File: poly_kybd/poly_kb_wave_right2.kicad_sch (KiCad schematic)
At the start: 47 parts, among them J37 FH34SRJ-12S-0.5SH, J38 Conn_01x05, J39 FH12-30S-0.5SH, SW1 RotaryEncoder_Switch, U2 TD6811, U3 MT9700

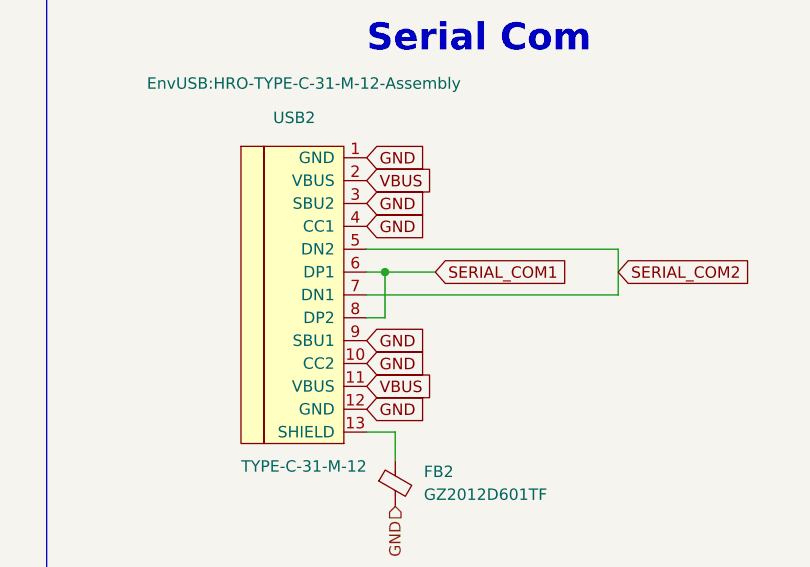
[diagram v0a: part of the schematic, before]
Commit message: Update PCB and plate to rev3 (disconnected vbus via bridge and removed polyfuse)
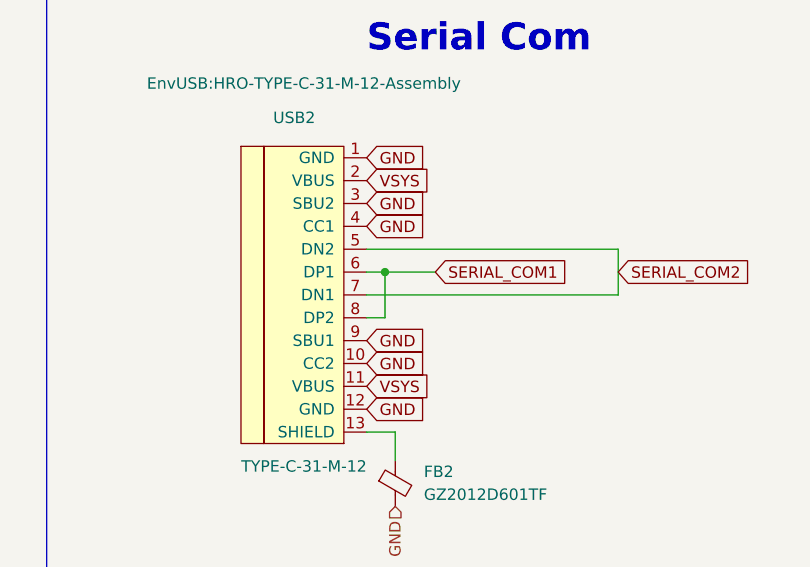
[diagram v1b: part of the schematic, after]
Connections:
- net VBUS: no longer USB2.11 (VBUS), USB2.2 (VBUS)
- net VSYS: now also USB2.11 (VBUS), USB2.2 (VBUS)
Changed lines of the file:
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@@
   (title_block
     (title "PolyKybd Split72 R")
-    (date "2023-06-22")
-    (rev "2.2")
+    (date "2023-09-19")
+    (rev "3")
   )
   (junction (at 259.08 219.075) (diameter 0) (color 0 0 0 0)
@@
     )
   )
-  (global_label "VBUS" (shape input) (at 410.21 358.14 0) (fields_autoplaced)
+  (global_label "VSYS" (shape input) (at 410.21 358.14 0) (fields_autoplaced)
     (effects (font (size 1.27 1.27)) (justify left))
-    (property "Intersheetrefs" "${INTERSHEET_REFS}" (at 417.5217 358.0606 0)
+    (property "Intersheetrefs" "${INTERSHEET_REFS}" (at 417.7914 358.14 0)
       (effects (font (size 1.27 1.27)) (justify left) hide)
     )
@@
     )
   )
-  (global_label "VBUS" (shape input) (at 410.21 381 0) (fields_autoplaced)
+  (global_label "VSYS" (shape input) (at 410.21 381 0) (fields_autoplaced)
     (effects (font (size 1.27 1.27)) (justify left))
-    (property "Intersheetrefs" "${INTERSHEET_REFS}" (at 417.5217 380.9206 0)
+    (property "Intersheetrefs" "${INTERSHEET_REFS}" (at 417.7914 381 0)
       (effects (font (size 1.27 1.27)) (justify left) hide)
     )

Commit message: Added latest gerber files, latest STLs and updated readme
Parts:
- R13: value 22k 0603 -> 12k 0603; JLC (none) -> C22790; MPN C31850 -> C22790
- R25: value 5.1K 0402 -> 10K 0402; MPN C25905 -> C25744
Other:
- note added: "Rset 27k -> ~250mA Max / Rset 22k -> ~310mA Max"
- note removed: "~250mA Max"
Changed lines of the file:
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@@
     (effects (font (size 3 3) (thickness 0.6) bold) (justify left bottom))
   )
-  (text "Increase for more current: Imax = 6.8k / RSet" (at 504.19 374.015 0)
+  (text "Increase for more current: Imax = 6.8k / RSet" (at 510.54 372.11 0)
     (effects (font (size 1.27 1.27) bold) (justify left bottom))
   )
@@
     (effects (font (size 3 3) (thickness 0.6) bold) (justify left bottom))
   )
-  (text "~250mA Max" (at 554.99 349.25 0)
+  (text "Rset 27k -> ~250mA Max / Rset 22k -> ~310mA Max" (at 500.38 375.285 0)
     (effects (font (size 1.27 1.27)) (justify left bottom))
   )
@@
       (effects (font (size 1.27 1.27)))
     )
-    (property "Value" "5.1K 0402" (at 490.855 369.57 90)
+    (property "Value" "10K 0402" (at 490.855 369.57 90)
       (effects (font (size 1.27 1.27)))
     )
@@
       (effects (font (size 1.27 1.27)) hide)
     )
-    (property "MPN" "C25905" (at 492.76 363.22 0)
+    (property "MPN" "C25744" (at 492.76 363.22 0)
       (effects (font (size 1.27 1.27)) hide)
     )
@@
       (effects (font (size 1.27 1.27)))
     )
-    (property "Value" "22k 0603" (at 503.555 369.57 90)
+    (property "Value" "12k 0603" (at 503.555 369.57 90)
       (effects (font (size 1.27 1.27)))
     )
@@
       (effects (font (size 1.27 1.27)) hide)
     )
-    (property "MPN" "C31850" (at 501.015 363.22 0)
+    (property "MPN" "C22790" (at 501.015 363.22 0)
       (effects (font (size 1.27 1.27)) hide)
     )
-    (property "JLC" "" (at 501.015 363.22 0)
+    (property "JLC" "C22790" (at 501.015 363.22 0)
       (effects (font (size 1.27 1.27)) hide)
     )
